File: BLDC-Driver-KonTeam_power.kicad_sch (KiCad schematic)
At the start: 68 parts, among them J1 HOA_Enable, J10 HOB_Enable, J11 LOB_Enable, J12 A, J13 B, J14 C, J2 Horn, J3 Logic_Conn, J4 Logic_Test, J6 IN, J7 LOC_Enable, J8 HOC_Enable, J9 LOA_Enable, Q1 IRFB7730, Q2 IRFB7730, Q3 IRFB7730, Q4 IRFB7730, Q5 IRFB7730, Q6 IRFB7730, U1 IR2101, U2 IR2101, U3 IR2101, U4 Buck Converter, U5 LM7805_TO220

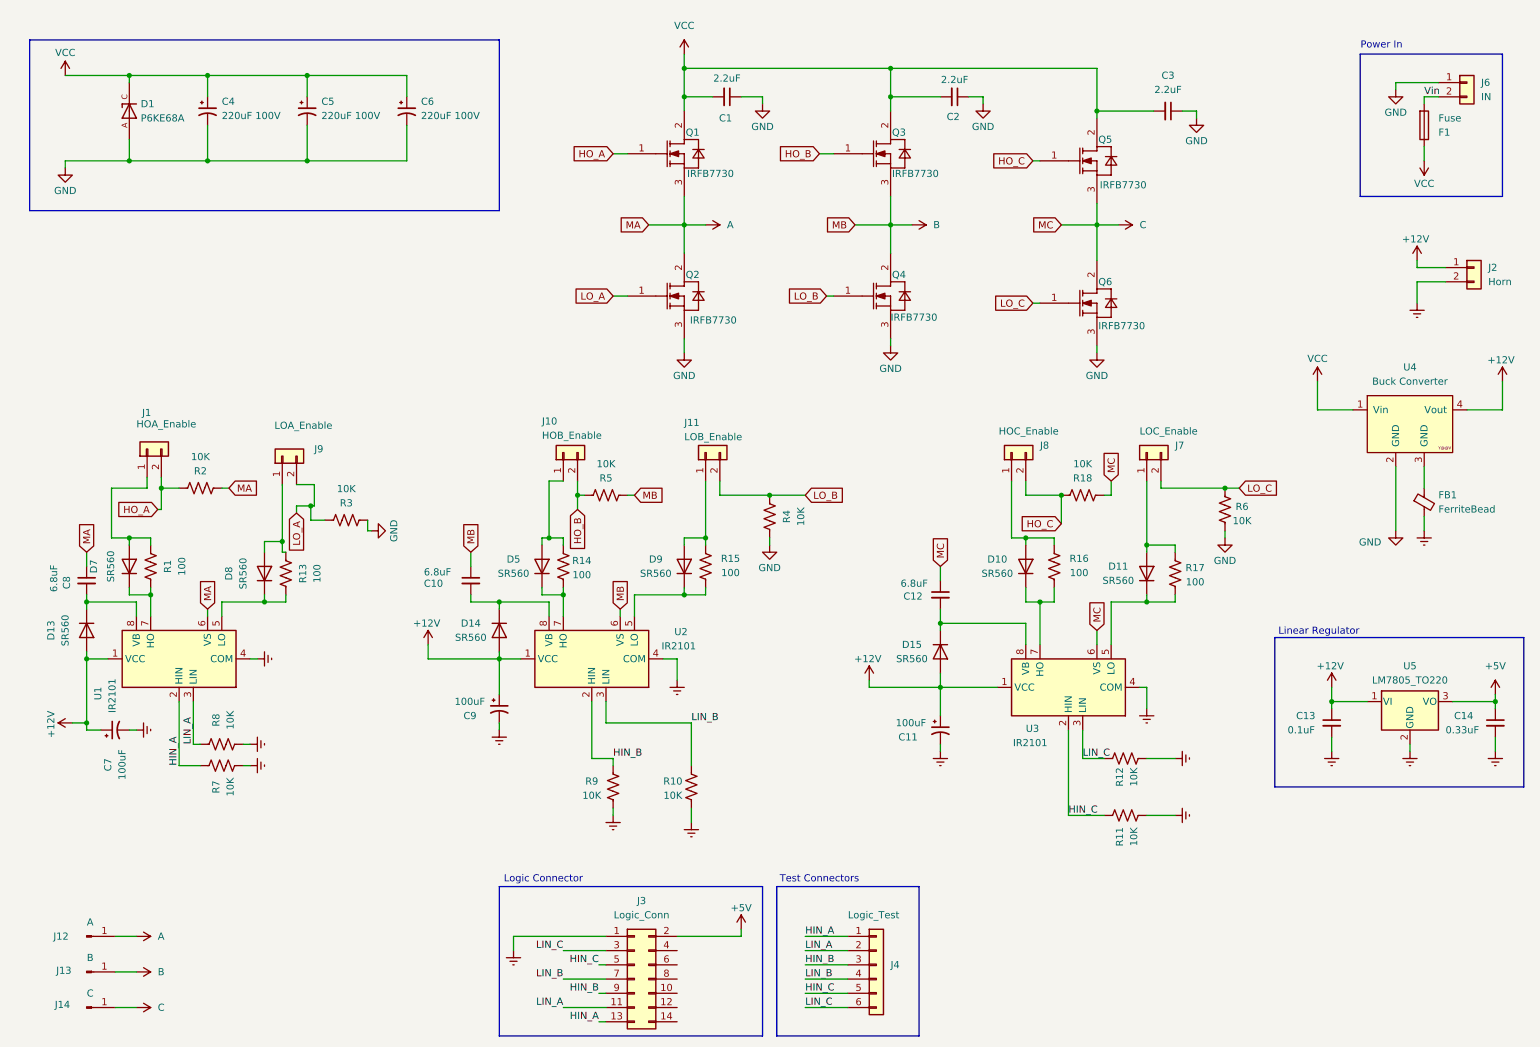
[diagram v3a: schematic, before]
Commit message: cambio de driver, cambio de mosfet , añadido aislamiento galvanico entre logica y potencia
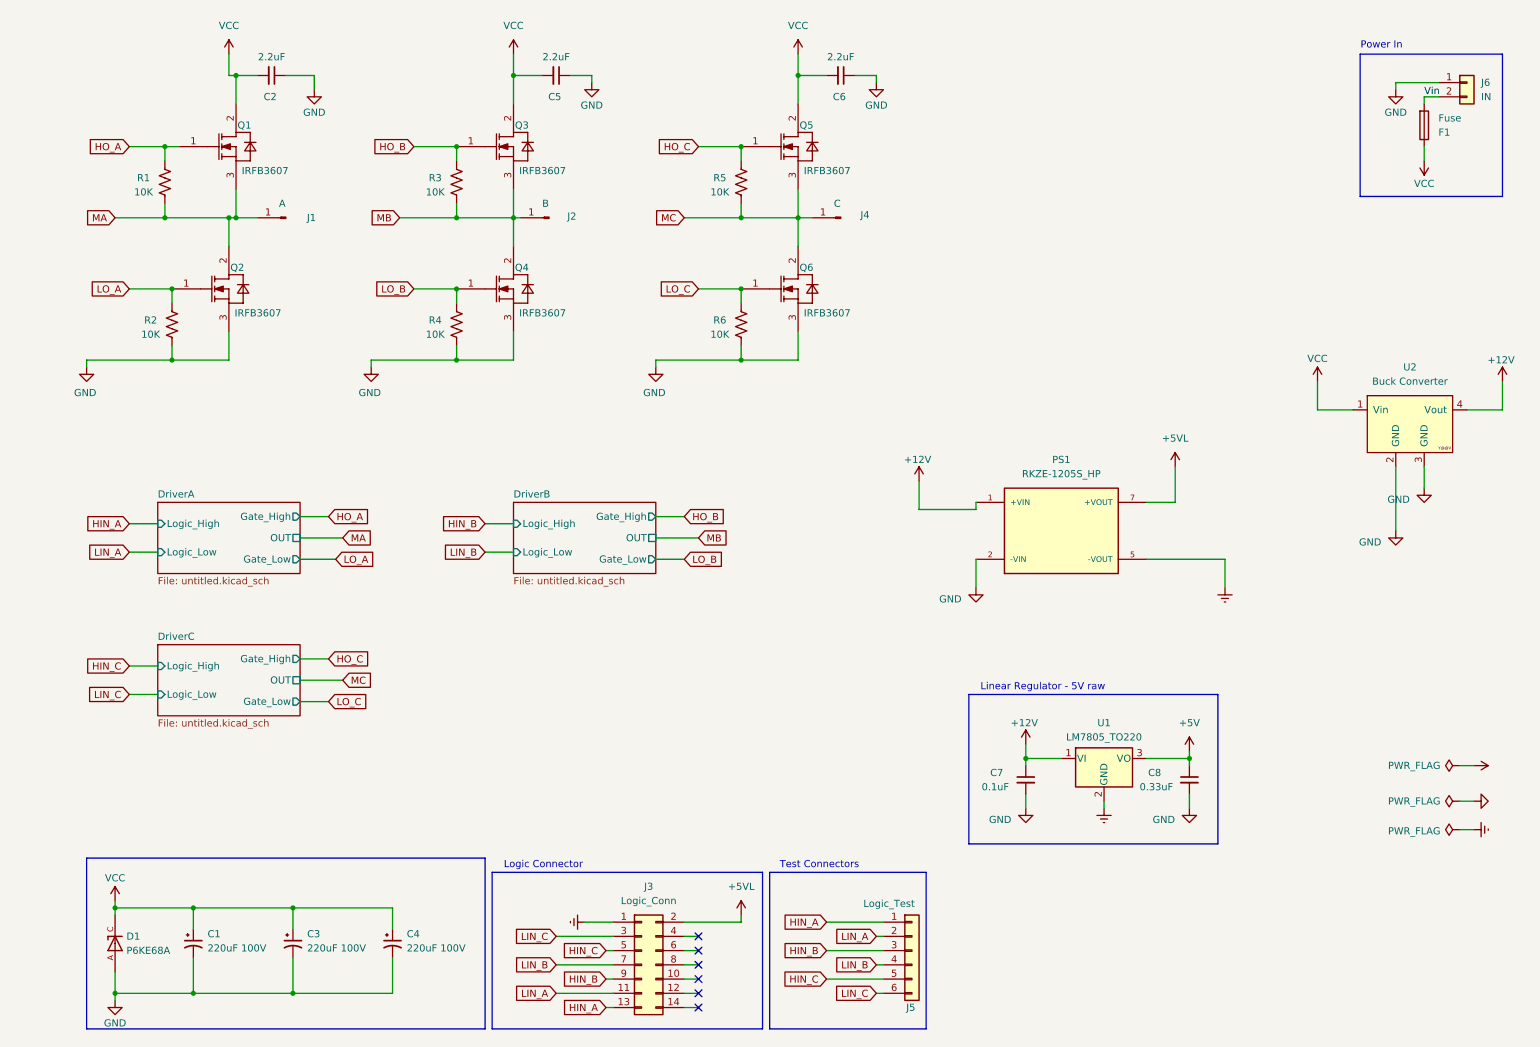
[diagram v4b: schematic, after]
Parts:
- removed C10, C12, C8: 6.8uF, Capacitor_THT:CP_Radial_Tantal_D4.5mm_P2.50mm, symbol Device:C_Small
- removed C11, C7, C9: 100uF, Capacitor_THT:C_Radial_D6.3mm_H11.0mm_P2.50mm, symbol Device:C_Polarized_Small_US
- removed C2, C3: 2.2uF, Capacitor_THT:C_Disc_D5.0mm_W2.5mm_P2.50mm, symbol Device:C_Small
- removed D10, D11, D13, D14, D15, D5, D7, D8, D9: SR560, Diode_THT:D_DO-35_SOD27_P7.62mm_Horizontal, symbol Diode:1N4001
- removed FB1: FerriteBead, Resistor_THT:R_Axial_DIN0204_L3.6mm_D1.6mm_P7.62mm_Horizontal, symbol Device:FerriteBead_Small
- removed J1: HOA_Enable, Connector_PinHeader_2.54mm:PinHeader_1x02_P2.54mm_Vertical, symbol Connector_Generic:Conn_01x02
- removed J10: HOB_Enable, Connector_PinHeader_2.54mm:PinHeader_1x02_P2.54mm_Vertical, symbol Connector_Generic:Conn_01x02
- removed J11: LOB_Enable, Connector_PinHeader_2.54mm:PinHeader_1x02_P2.54mm_Vertical, symbol Connector_Generic:Conn_01x02
- removed J2: Horn, Connector_AMASS:AMASS_XT60-F_1x02_P7.20mm_Vertical, symbol Connector_Generic:Conn_01x02
- removed J7: LOC_Enable, Connector_PinHeader_2.54mm:PinHeader_1x02_P2.54mm_Vertical, symbol Connector_Generic:Conn_01x02
- removed J8: HOC_Enable, Connector_PinHeader_2.54mm:PinHeader_1x02_P2.54mm_Vertical, symbol Connector_Generic:Conn_01x02
- removed J9: LOA_Enable, Connector_PinHeader_2.54mm:PinHeader_1x02_P2.54mm_Vertical, symbol Connector_Generic:Conn_01x02
- removed R1, R13, R14, R15, R16, R17: 100, Resistor_THT:R_Axial_DIN0204_L3.6mm_D1.6mm_P7.62mm_Horizontal, symbol Device:R_US
- removed R10, R11, R12, R18, R7, R8, R9: 10K, Resistor_THT:R_Axial_DIN0204_L3.6mm_D1.6mm_P7.62mm_Horizontal, symbol Device:R_US
- removed U1, U2, U3: IR2101, Package_DIP:DIP-8_W7.62mm_LongPads, symbol Driver_FET:IR2101
- added C5, C6: 2.2uF, Capacitor_SMD:C_0805_2012Metric_Pad1.18x1.45mm_HandSolder, symbol Device:C_Small
- added PS1: RKZE-1205S_HP, KON:CONV_RKZE-1205S_HP, symbol RKZE-1205S_HP:RKZE-1205S_HP
- added R4: 10K, Resistor_SMD:R_0805_2012Metric_Pad1.20x1.40mm_HandSolder, symbol Device:R_US
- C2: renamed from C1; footprint Capacitor_THT:C_Disc_D5.0mm_W2.5mm_P2.50mm -> Capacitor_SMD:C_0805_2012Metric_Pad1.18x1.45mm_HandSolder
- D1: footprint P6KE68A:DIOAD1300W80L670D310 -> KON:DIOAD1300W80L670D310
- Q1, Q2, Q3, Q4, Q5, Q6: value IRFB7730 -> IRFB3607; footprint kicad:IRFB7730 -> KON:TO254P1016X419X2286-3
- R1: renamed from R4; footprint Resistor_THT:R_Axial_DIN0204_L3.6mm_D1.6mm_P7.62mm_Horizontal -> Resistor_SMD:R_0805_2012Metric_Pad1.20x1.40mm_HandSolder
- R2, R3, R5, R6: footprint Resistor_THT:R_Axial_DIN0204_L3.6mm_D1.6mm_P7.62mm_Horizontal -> Resistor_SMD:R_0805_2012Metric_Pad1.20x1.40mm_HandSolder
- U2: renamed from U4; footprint KiCad:YAAJ_DCDC_StepDown_LM2596 -> KON:DC_DC_LM2596_small
- renumbered C4 to C1, C5 to C3, C6 to C4, C13 to C7, C14 to C8, J12 to J1, J13 to J2, J14 to J4, J4 to J5, U5 to U1
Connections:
- net +12V: now also PS1.1 (+VIN)
- net +5V: no longer J3.2 (Pin_2)
- net Earth: now also PS1.5 (-VOUT); no longer C7.2, C8.2
- net GND: now also C7.2, C8.2, R2.1, R6.1, U2.3 (GND), C5.1, C6.1, PS1.2 (-VIN), R4.1; no longer R1.2, R3.2, R6.2
- net HO_A: now also R1.2; no longer R2.1
- net HO_B: now also R3.2; no longer R5.1
- net HO_C: now also R5.2
- net LO_A: now also R2.2; no longer R3.1
- net LO_B: now also R4.2; no longer R1.1
- net LO_C: now also R6.2; no longer R6.1
- net VCC: now also C5.2, C6.2
- net A renamed MA
- net MA: now also R1.1; no longer R2.2
- net B renamed MB
- net MB: now also R3.1; no longer R5.2
- net C renamed MC
- net MC: now also R5.1
- new net +5VL: J3.2 (Pin_2), PS1.7 (+VOUT)
- no-connect marks 0 -> 6
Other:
- added sheet DriverA (untitled.kicad_sch)
- added sheet DriverB (untitled.kicad_sch)
- added sheet DriverC (untitled.kicad_sch)
- note added: "Linear Regulator - 5V raw"
- note removed: "Linear Regulator"
- moved on the sheet: C1, C2, C3, C4, C7, C8, D1, J1, J2, J3, J4, J5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

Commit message: correciones( aislamiento LM7805) , cambio de ID , primer ruteo
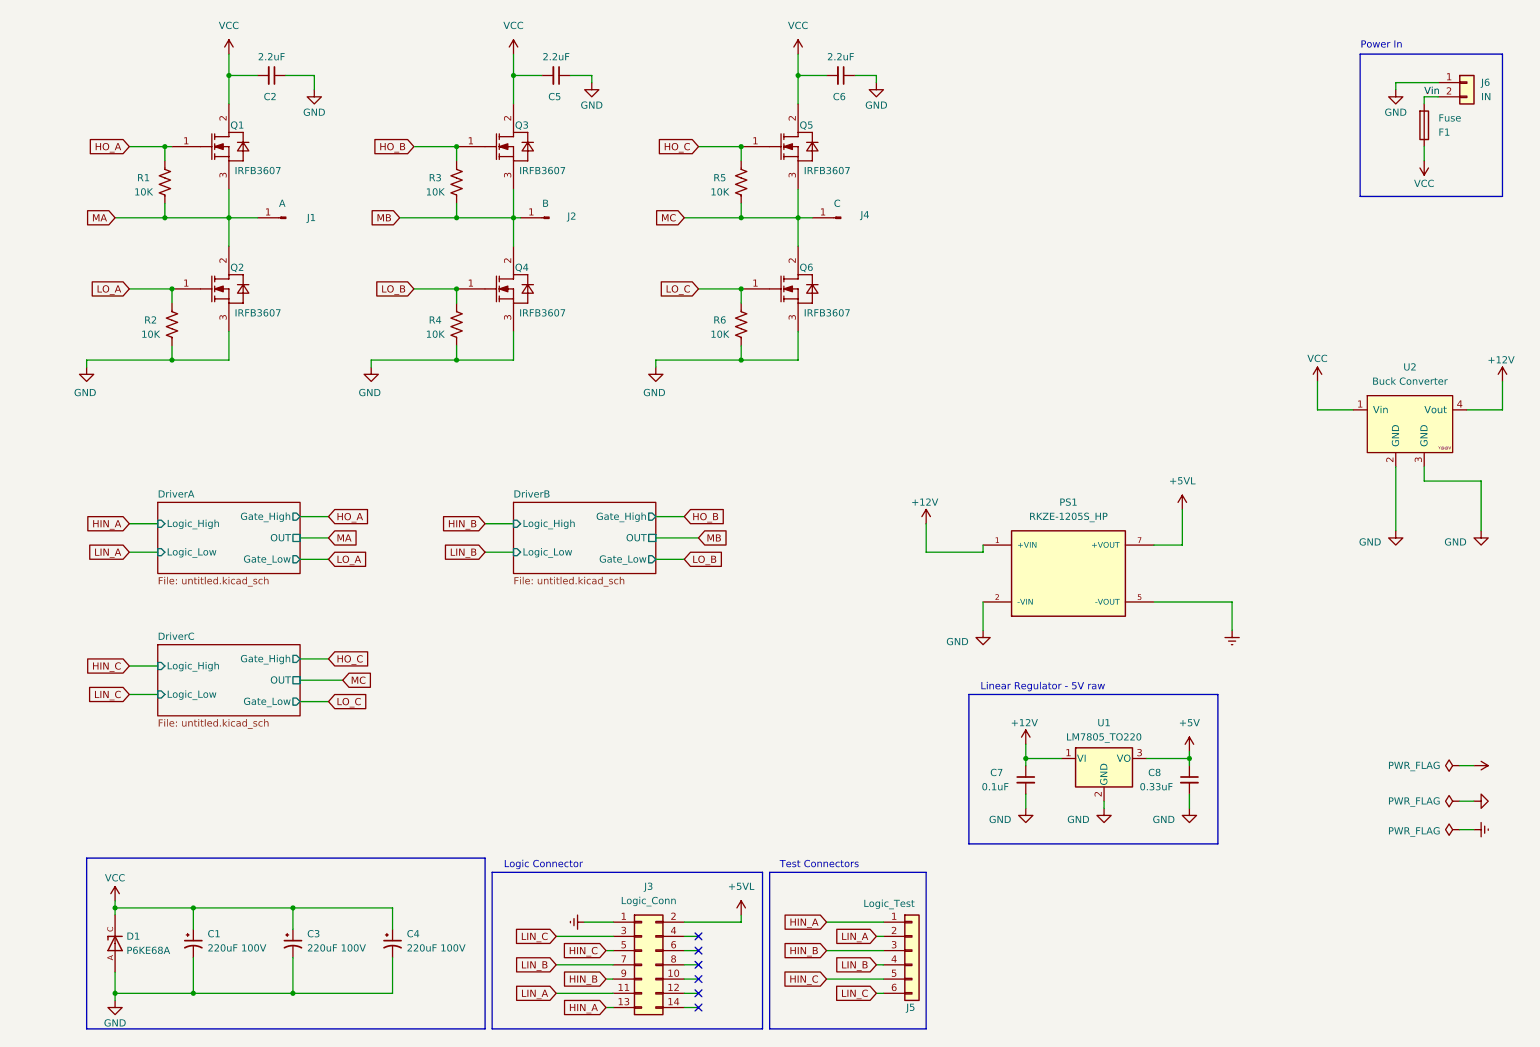
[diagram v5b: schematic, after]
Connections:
- net Earth: no longer U1.2 (GND)
- net GND: now also U1.2 (GND)
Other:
- moved on the sheet: PS1, Q1
